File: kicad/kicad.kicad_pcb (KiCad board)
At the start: 2 copper layers, 2 parts

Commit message: Got OLED working
and the UI works like I want too
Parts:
- added REF**: Pin_D0.7mm_L6.5mm_W1.8mm_FlatFork, Connector_Pin:Pin_D0.7mm_L6.5mm_W1.8mm_FlatFork, F.Cu at (170.2, 68.6)
- added REF**: Pin_D0.7mm_L6.5mm_W1.8mm_FlatFork, Connector_Pin:Pin_D0.7mm_L6.5mm_W1.8mm_FlatFork, F.Cu at (180.3, 68.6)
- added REF**: C_Disc_D9.0mm_W5.0mm_P10.00mm, Capacitor_THT:C_Disc_D9.0mm_W5.0mm_P10.00mm, F.Cu at (160.1, 76.2)
- added REF**: Pin_D0.7mm_L6.5mm_W1.8mm_FlatFork, Connector_Pin:Pin_D0.7mm_L6.5mm_W1.8mm_FlatFork, F.Cu at (170.2, 104.1)
- added REF**: Pin_D0.7mm_L6.5mm_W1.8mm_FlatFork, Connector_Pin:Pin_D0.7mm_L6.5mm_W1.8mm_FlatFork, F.Cu at (180.3, 88.9)
- added REF**: Pin_D0.7mm_L6.5mm_W1.8mm_FlatFork, Connector_Pin:Pin_D0.7mm_L6.5mm_W1.8mm_FlatFork, F.Cu at (180.3, 104.1)
- added REF**: C_Disc_D9.0mm_W5.0mm_P10.00mm, Capacitor_THT:C_Disc_D9.0mm_W5.0mm_P10.00mm, F.Cu at (160.0, 96.5)
- added REF**: Pin_D0.7mm_L6.5mm_W1.8mm_FlatFork, Connector_Pin:Pin_D0.7mm_L6.5mm_W1.8mm_FlatFork, F.Cu at (170.2, 88.9)
- added REF**: Pin_D0.7mm_L6.5mm_W1.8mm_FlatFork, Connector_Pin:Pin_D0.7mm_L6.5mm_W1.8mm_FlatFork, F.Cu at (180.3, 83.8)
- added REF**: Pin_D0.7mm_L6.5mm_W1.8mm_FlatFork, Connector_Pin:Pin_D0.7mm_L6.5mm_W1.8mm_FlatFork, F.Cu at (170.2, 83.8)
- moved REF** 99.0 mm to (185.8, 83.9)
- moved REF** 90.2 mm to (140.1, 63.5)
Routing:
- net (no net): track 41.9 -> 351.0 mm

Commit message: wip
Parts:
- removed the REF** at (170.2, 68.6)
- removed the REF** at (180.3, 68.6)
- removed the REF** at (160.1, 76.2)
- removed the REF** at (170.2, 104.1)
- removed the REF** at (180.3, 88.9)
- removed the REF** at (180.3, 104.1)
- removed the REF** at (160.0, 96.5)
- removed the REF** at (170.2, 88.9)
- removed the REF** at (180.3, 83.8)
- removed the REF** at (170.2, 83.8)
- removed the REF** at (185.8, 83.9)
- added 1: , Connector_Pin:Pin_D0.7mm_L6.5mm_W1.8mm_FlatFork, F.Cu at (134.6, 124.5)
- added 1: , Connector_Pin:Pin_D0.7mm_L6.5mm_W1.8mm_FlatFork, F.Cu at (137.2, 124.5)
- added 1: , Connector_Pin:Pin_D0.7mm_L6.5mm_W1.8mm_FlatFork, F.Cu at (142.2, 111.8)
- added 1: , Connector_Pin:Pin_D0.7mm_L6.5mm_W1.8mm_FlatFork, F.Cu at (142.2, 124.5)
- added 1: , Connector_Pin:Pin_D0.7mm_L6.5mm_W1.8mm_FlatFork, F.Cu at (116.8, 88.9)
- added 1: , Connector_Pin:Pin_D0.7mm_L6.5mm_W1.8mm_FlatFork, F.Cu at (142.2, 119.4)
- added 1: , Connector_Pin:Pin_D0.7mm_L6.5mm_W1.8mm_FlatFork, F.Cu at (144.8, 119.4)
- added 1: , Connector_Pin:Pin_D0.7mm_L6.5mm_W1.8mm_FlatFork, F.Cu at (139.7, 119.4)
- added 1: , Connector_Pin:Pin_D0.7mm_L6.5mm_W1.8mm_FlatFork, F.Cu at (116.8, 96.5)
- added 1: , Connector_Pin:Pin_D0.7mm_L6.5mm_W1.8mm_FlatFork, F.Cu at (139.7, 111.8)
- added 1: , Connector_Pin:Pin_D0.7mm_L6.5mm_W1.8mm_FlatFork, F.Cu at (144.8, 124.5)
- added 1: , Connector_Pin:Pin_D0.7mm_L6.5mm_W1.8mm_FlatFork, F.Cu at (132.1, 124.5)
- added 1: , Connector_Pin:Pin_D0.7mm_L6.5mm_W1.8mm_FlatFork, F.Cu at (139.7, 124.5)
- added 1: , Connector_Pin:Pin_D0.7mm_L6.5mm_W1.8mm_FlatFork, F.Cu at (147.3, 124.5)
- added 1: , Connector_Pin:Pin_D0.7mm_L6.5mm_W1.8mm_FlatFork, F.Cu at (134.6, 91.4)
- added 1: , Connector_Pin:Pin_D0.7mm_L6.5mm_W1.8mm_FlatFork, F.Cu at (149.9, 124.5)
- added 1: , Connector_Pin:Pin_D0.7mm_L6.5mm_W1.8mm_FlatFork, F.Cu at (144.8, 111.8)
- added 2: , Connector_Pin:Pin_D0.7mm_L6.5mm_W1.8mm_FlatFork, F.Cu at (137.2, 91.4)
- added 3: , Connector_Pin:Pin_D0.7mm_L6.5mm_W1.8mm_FlatFork, F.Cu at (139.7, 91.4)
- added 4: , Connector_Pin:Pin_D0.7mm_L6.5mm_W1.8mm_FlatFork, F.Cu at (142.2, 91.4)
- added ?: , , F.Cu at (167.6, 124.5)
- added ?: , , F.Cu at (109.2, 124.5)
- added REF**: MountingHole_2.2mm_M2_ISO7380_Pad, MountingHole:MountingHole_2.2mm_M2_ISO7380_Pad, F.Cu at (167.6, 78.7)
- added REF**: MountingHole_2.2mm_M2_ISO7380_Pad, MountingHole:MountingHole_2.2mm_M2_ISO7380_Pad, F.Cu at (109.2, 78.7)
- REF**: moved to B.Cu
- moved REF** 40.3 mm to (116.8, 96.5), turned to -90 degrees
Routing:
- net (no net): track 351.0 -> 525.6 mm, vias 0 -> 2
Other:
- board outline added: 63.5 x 50.8 mm

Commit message: added web page
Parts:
- removed the 1 at (134.6, 124.5)
- removed the 1 at (137.2, 124.5)
- removed the 1 at (142.2, 111.8)
- removed the 1 at (142.2, 124.5)
- removed the 1 at (142.2, 119.4)
- removed the 1 at (144.8, 119.4)
- removed the 1 at (139.7, 111.8)
- removed the 1 at (144.8, 124.5)
- removed the 1 at (132.1, 124.5)
- removed the 1 at (139.7, 124.5)
- removed the 1 at (147.3, 124.5)
- removed the 1 at (134.6, 91.4)
- removed the 1 at (149.9, 124.5)
- removed the 1 at (144.8, 111.8)
- removed 2, 3, 4: , Connector_Pin:Pin_D0.7mm_L6.5mm_W1.8mm_FlatFork
- added ?: , Connector_Pin:Pin_D0.7mm_L6.5mm_W1.8mm_FlatFork, F.Cu at (127.0, 124.5)
- added ?: , , F.Cu at (142.2, 91.4)
- added ?: , Connector_Pin:Pin_D0.7mm_L6.5mm_W1.8mm_FlatFork, F.Cu at (142.2, 124.5)
- added ?: , Connector_Pin:Pin_D0.7mm_L6.5mm_W1.8mm_FlatFork, F.Cu at (134.6, 119.4)
- added ?: , , F.Cu at (139.7, 91.4)
- added ?: , Connector_Pin:Pin_D0.7mm_L6.5mm_W1.8mm_FlatFork, F.Cu at (132.1, 111.8)
- added ?: , Connector_Pin:Pin_D0.7mm_L6.5mm_W1.8mm_FlatFork, F.Cu at (124.5, 124.5)
- added ?: , Connector_Pin:Pin_D0.7mm_L6.5mm_W1.8mm_FlatFork, F.Cu at (152.4, 124.5)
- added ?: , Connector_Pin:Pin_D0.7mm_L6.5mm_W1.8mm_FlatFork, F.Cu at (134.6, 124.5)
- added ?: , Connector_Pin:Pin_D0.7mm_L6.5mm_W1.8mm_FlatFork, F.Cu at (149.9, 124.5)
- added ?: , , F.Cu at (134.6, 91.4)
- added ?: , Connector_Pin:Pin_D0.7mm_L6.5mm_W1.8mm_FlatFork, F.Cu at (129.5, 124.5)
- added ?: , Connector_Pin:Pin_D0.7mm_L6.5mm_W1.8mm_FlatFork, F.Cu at (147.3, 124.5)
- added ?: , Connector_Pin:Pin_D0.7mm_L6.5mm_W1.8mm_FlatFork, F.Cu at (137.2, 111.8)
- added ?: , Connector_Pin:Pin_D0.7mm_L6.5mm_W1.8mm_FlatFork, F.Cu at (137.2, 119.4)
- added ?: , , F.Cu at (137.2, 91.4)
- added ?: , Connector_Pin:Pin_D0.7mm_L6.5mm_W1.8mm_FlatFork, F.Cu at (137.2, 124.5)
- added ?: , Connector_Pin:Pin_D0.7mm_L6.5mm_W1.8mm_FlatFork, F.Cu at (144.8, 124.5)
- added ?: , Connector_Pin:Pin_D0.7mm_L6.5mm_W1.8mm_FlatFork, F.Cu at (139.7, 124.5)
- added ?: , Connector_Pin:Pin_D0.7mm_L6.5mm_W1.8mm_FlatFork, F.Cu at (132.1, 124.5)
- added ?: , Connector_Pin:Pin_D0.7mm_L6.5mm_W1.8mm_FlatFork, F.Cu at (134.6, 111.8)
- moved ? 7.62 mm to (132.1, 119.4)
- moved REF** 5.08 mm to (116.8, 101.6)
- renumbered 1 to ?
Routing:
- net (no net): track 525.6 -> 612.7 mm, vias 2 -> 1

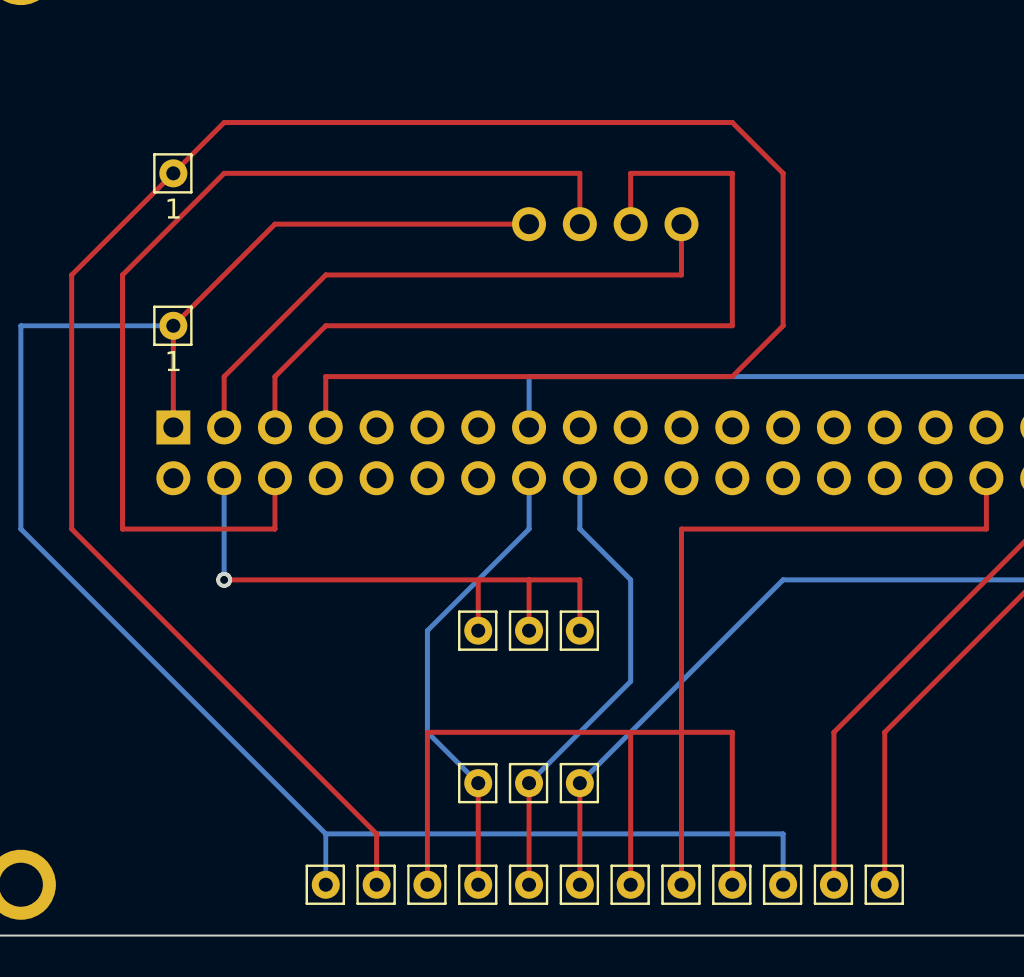
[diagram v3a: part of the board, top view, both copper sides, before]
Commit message: fixed mistake in pcb (display was all wrong)
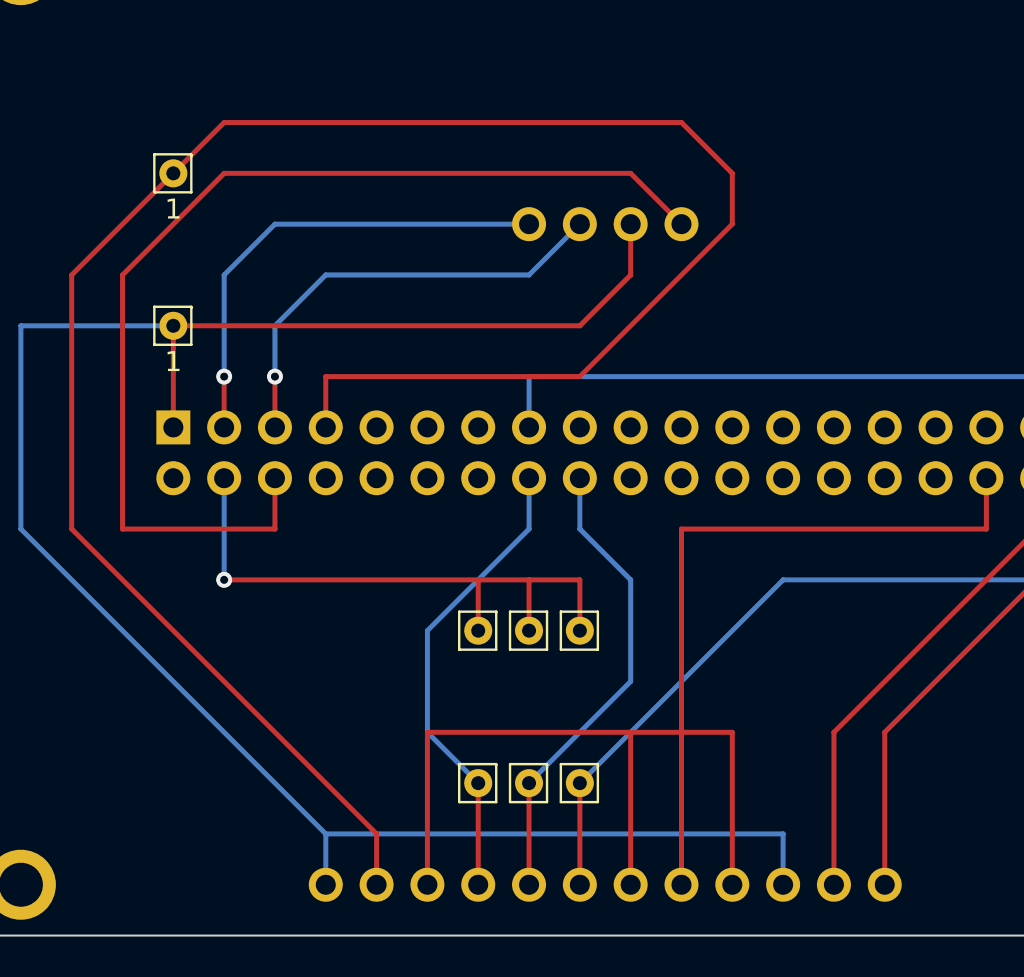
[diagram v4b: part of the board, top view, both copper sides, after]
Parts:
- removed the ? at (127.0, 124.5)
- removed the ? at (142.2, 124.5)
- removed the ? at (124.5, 124.5)
- removed the ? at (152.4, 124.5)
- removed the ? at (134.6, 124.5)
- removed the ? at (149.9, 124.5)
- removed the ? at (129.5, 124.5)
- removed the ? at (147.3, 124.5)
- removed the ? at (137.2, 124.5)
- removed the ? at (144.8, 124.5)
- removed the ? at (139.7, 124.5)
- removed the ? at (132.1, 124.5)
- added ?: , , F.Cu at (152.4, 124.5)
- added ?: , , F.Cu at (142.2, 124.5)
- added ?: , , F.Cu at (132.1, 124.5)
- added ?: , , F.Cu at (127.0, 124.5)
- added ?: , , F.Cu at (149.9, 124.5)
- added ?: , , F.Cu at (124.5, 124.5)
- added ?: , , F.Cu at (144.8, 124.5)
- added ?: , , F.Cu at (134.6, 124.5)
- added ?: , , F.Cu at (129.5, 124.5)
- added ?: , , F.Cu at (139.7, 124.5)
- added ?: , , F.Cu at (147.3, 124.5)
- added ?: , , F.Cu at (137.2, 124.5)
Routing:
- net (no net): track 612.7 -> 589.4 mm, vias 1 -> 3

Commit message: rev 5 of kicad board
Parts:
- moved REF** 5.68 mm to (111.8, 104.1)
- moved 1 2.54 mm to (116.8, 86.4)
- moved ? 1.27 mm to (134.6, 120.7)
- moved ? 1.27 mm to (132.1, 120.7)
- moved ? 1.27 mm to (137.2, 120.7)
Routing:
- net (no net): track 589.4 -> 576.8 mm
